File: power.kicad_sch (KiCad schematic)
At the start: 33 parts, among them U6 TLV62569DBV, U8 TPS63070RNMR, U9 TPS2121RUXR

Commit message: Route some peripherals
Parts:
- R29, R30: footprint Resistor_SMD:R_0402_1005Metric -> Resistor_SMD:R_0201_0603Metric
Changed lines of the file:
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@@
 			)
 		)
-		(property "Footprint" "Resistor_SMD:R_0402_1005Metric"
+		(property "Footprint" "Resistor_SMD:R_0201_0603Metric"
 			(at 57.658 44.45 90)
 			(hide yes)
@@
 			)
 		)
-		(property "Footprint" "Resistor_SMD:R_0402_1005Metric"
+		(property "Footprint" "Resistor_SMD:R_0201_0603Metric"
 			(at 57.658 54.61 90)
 			(hide yes)

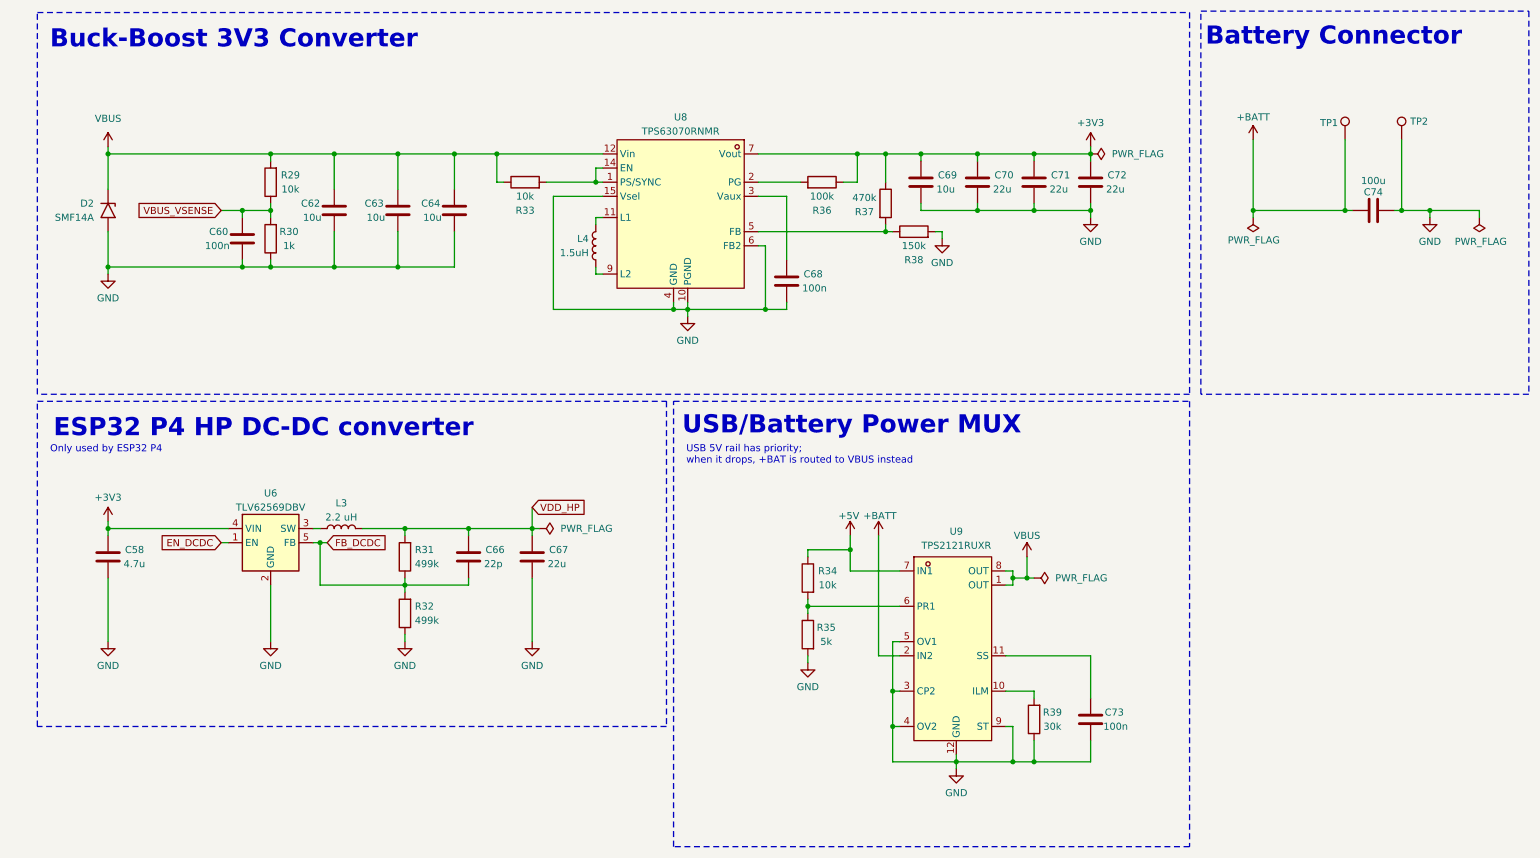
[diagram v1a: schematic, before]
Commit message: Remove external SPI connections and switch voltage measurement from VBUS to +BAT
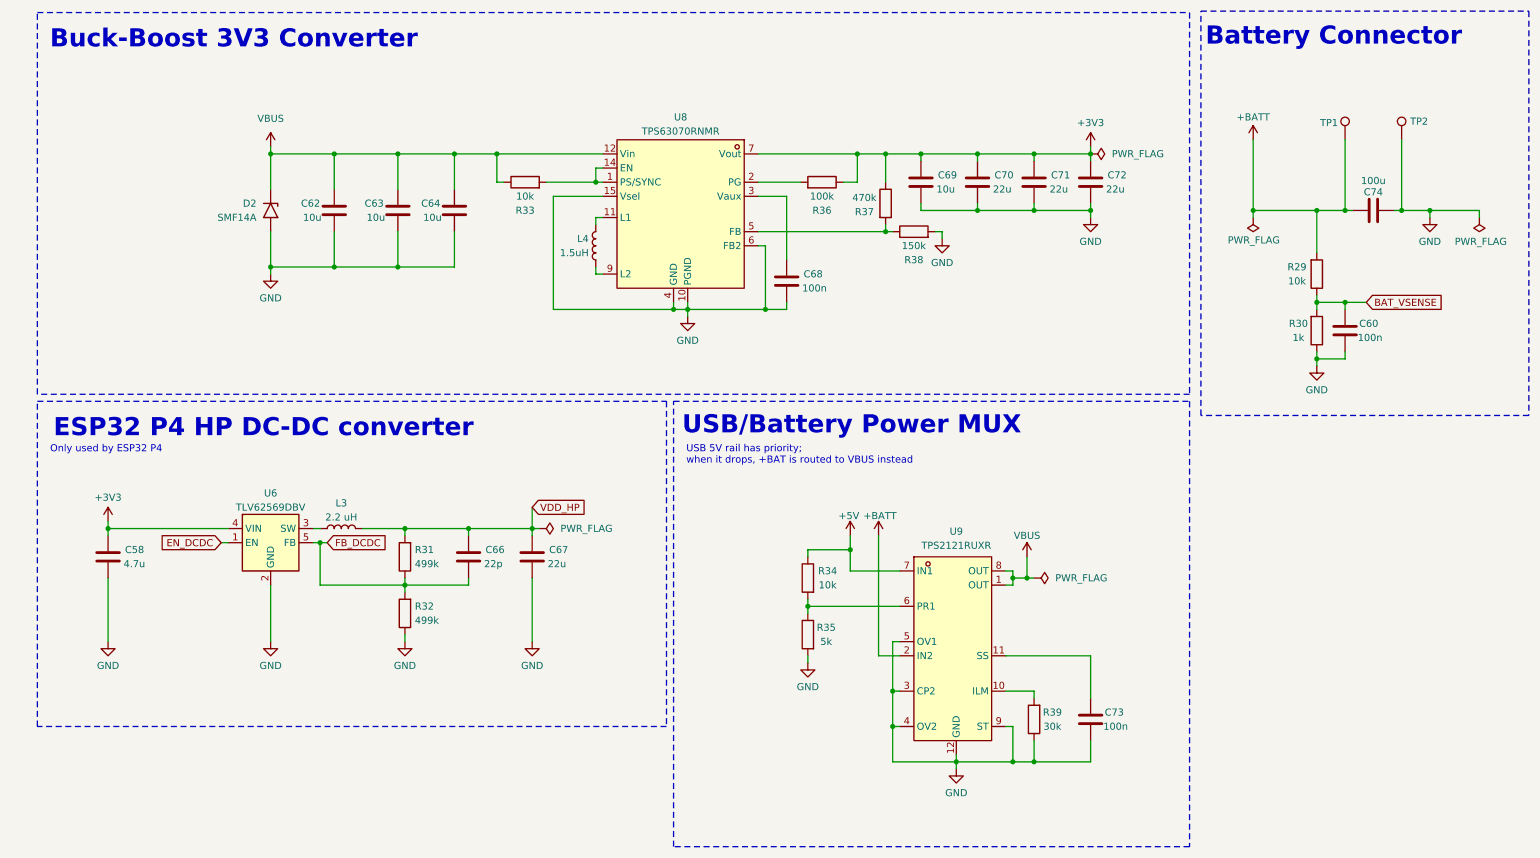
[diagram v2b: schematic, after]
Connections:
- net +BATT: now also R29.2
- net VBUS: no longer R29.2
- net VBUS_VSENSE renamed BAT_VSENSE
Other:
- moved on the sheet: D2

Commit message: Clean up schematics a bit
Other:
- note added: "The 3V3 converter is fed from USB 5V with priority; when it drops, +BAT is routed to VBUS instead"
- note removed: "USB 5V rail has priority; when it drops, +BAT is routed to VBUS instead"
- moved on the sheet: C58, C62, C63, C64, C66, C67, C68, C69, C70, C71, C72, D2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

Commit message: Minimize passive footprints again and switch ESC mcu to smaller footprint
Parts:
- removed C62, C63, C64: 10u, Capacitor_SMD:C_0805_2012Metric, symbol Device:C
- removed C68: 100n, Capacitor_SMD:C_0402_1005Metric, symbol Device:C
- removed C69: 10u, Capacitor_SMD:C_0603_1608Metric, symbol Device:C
- removed C70, C71, C72: 22u, Capacitor_SMD:C_0603_1608Metric, symbol Device:C
- removed C74: 100u, Capacitor_SMD:C_1206_3216Metric, symbol Device:C
- removed D2: SMF14A, Diode_SMD:D_SMF, symbol Diode:SMF14A
- removed L4: 1.5uH, Inductor_SMD:L_Coilcraft_XxL4020, symbol Device:L
- removed R33: 10k, Resistor_SMD:R_0402_1005Metric, symbol Device:R
- removed R36: 100k, Resistor_SMD:R_0402_1005Metric, symbol Device:R
- removed R37: 470k, Resistor_SMD:R_0402_1005Metric, symbol Device:R
- removed R38: 150k, Resistor_SMD:R_0402_1005Metric, symbol Device:R
- removed U8: TPS63070RNMR, easyeda2kicad:VQFN-15_L3.0-W2.5-P0.50-BL, symbol easyeda2kicad:TPS63070RNMR
- added C65: 6.8n, Capacitor_SMD:C_0201_0603Metric, symbol Device:C
- added C76: 100n, Capacitor_SMD:C_0402_1005Metric, symbol Device:C
- added C77, C78: 22u, Capacitor_SMD:C_0805_2012Metric, symbol Device:C
- added C79, C80: 10u, Capacitor_SMD:C_0805_2012Metric, symbol Device:C
- added D3: SMF14A, Diode_SMD:D_SMF, symbol Diode:SMF14A
- added L5: 1.5uH, Inductor_SMD:L_1008_2520Metric, symbol Device:L
- added R40: 31.3k, Resistor_SMD:R_0201_0603Metric, symbol Device:R
- added R41, R42: 10k, Resistor_SMD:R_0201_0603Metric, symbol Device:R
- added U17: TPS62933, Package_TO_SOT_SMD:SOT-583-8, symbol Regulator_Switching:TPS62933
- C58: value 4.7u -> 10u
- C66, C73: footprint Capacitor_SMD:C_0402_1005Metric -> Capacitor_SMD:C_0201_0603Metric
- R31, R32, R34, R35, R39: footprint Resistor_SMD:R_0402_1005Metric -> Resistor_SMD:R_0201_0603Metric
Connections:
- net +3V3: now also C77.2, C78.2, L5.2, R40.1
- net GND: now also C65.2, C77.1, C78.1, C79.2, C80.2, D3.2 (A2), R41.1, U17.4 (GND)
- net VBUS: now also C79.1, C80.1, D3.1 (A1), R42.2, U17.3 (VIN)
- new net: R40.2, R41.2, U17.8 (FB)
- new net: R42.1, U17.1 (RT)
- new net: C76.2, L5.1, U17.5 (SW)
- new net: C76.1, U17.6 (BST)
- new net: C65.1, U17.7 (SS)
- no-connect marks 0 -> 1
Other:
- note added: "Buck 3V3 Converter"
- note added: "EN has internal pullup"
- note removed: "Buck-Boost 3V3 Converter"
- moved on the sheet: TP1, TP2

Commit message: Start laying out FC section
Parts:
- L3: footprint Inductor_SMD:L_Coilcraft_XAL4020-XXX -> easyeda2kicad:L0806
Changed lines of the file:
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@@
 			)
 		)
-		(property "Footprint" "Inductor_SMD:L_Coilcraft_XAL4020-XXX"
+		(property "Footprint" "easyeda2kicad:L0806"
 			(at 69.85 118.11 0)
 			(hide yes)

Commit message: Split FC stuff into subgroups
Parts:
- C60: footprint Capacitor_SMD:C_0402_1005Metric -> Capacitor_SMD:C_0201_0603Metric
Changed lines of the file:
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@@
 			)
 		)
-		(property "Footprint" "Capacitor_SMD:C_0402_1005Metric"
+		(property "Footprint" "Capacitor_SMD:C_0201_0603Metric"
 			(at 249.8852 74.93 0)
 			(hide yes)

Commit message: Good placement of most FC components
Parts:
- added C61: 100n, Capacitor_SMD:C_0201_0603Metric, symbol Device:C
- added R3: BVN-Z-R0005-1.0, easyeda2kicad:RES-SMD_4P-L4.1-W3.1-BL_BVN-1216, symbol easyeda2kicad:BVN-Z-R0005-1.0
- added R43: 1k, Resistor_SMD:R_0201_0603Metric, symbol Device:R
- added U8: INA190A2IDCKR, easyeda2kicad:SC-70-6_L2.0-W1.3-P0.65-LS2.1-BR, symbol easyeda2kicad:INA190A2IDCKR
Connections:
- net +3V3: now also C61.1, U8.3 (VS)
- net +BATT: now also R3.2; no longer TP1.1
- net GND: now also C61.2, U8.1 (REF), U8.2 (GND)
- new net: R3.3, U8.4 (IN+)
- new net: R3.4, U8.5 (IN-)
- new net: R43.1, U8.6 (OUT)
- new net: R3.1, TP1.1
- new net BAT_ISENSE: R43.2
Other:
- moved on the sheet: C60, C73, R29, R30, R34, R35, R39, TP1, TP2, U9

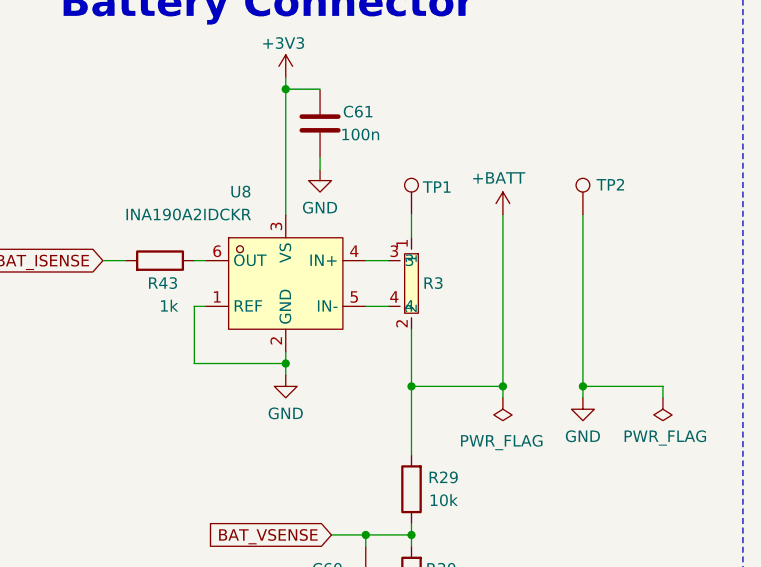
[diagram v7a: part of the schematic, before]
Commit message: Route MIPI-CSI
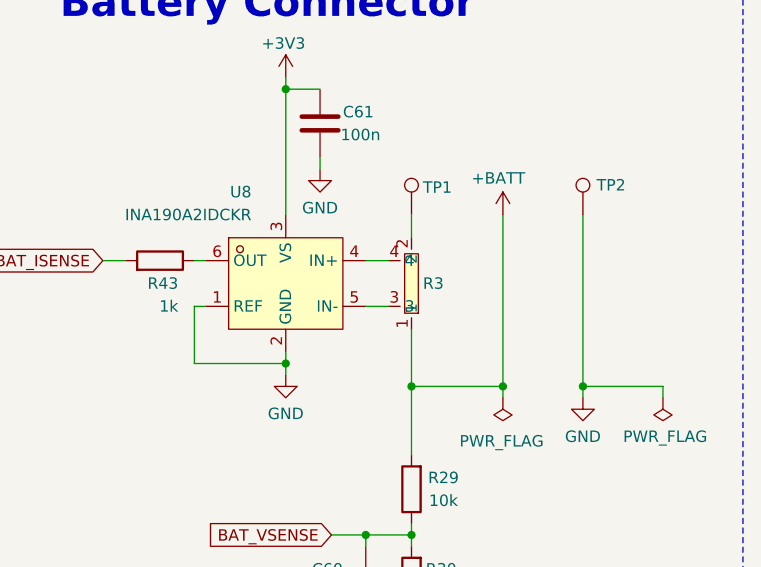
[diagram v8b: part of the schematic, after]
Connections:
- net +BATT: now also R3.1; no longer R3.2
- net at U8.4 (IN+): now also R3.4; no longer R3.3
- net at U8.5 (IN-): now also R3.3; no longer R3.4
- net at TP1.1: now also R3.2; no longer R3.1
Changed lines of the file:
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@@
 		(lib_id "easyeda2kicad:BVN-Z-R0005-1.0")
 		(at 243.84 49.53 270)
+		(mirror x)
 		(unit 1)
 		(body_style 1)
@@
 		)
 		(property "Value" "BVN-Z-R0005-1.0"
-			(at 247.65 48.2601 90)
+			(at 247.65 50.7999 90)
 			(hide yes)
 			(show_name no)
